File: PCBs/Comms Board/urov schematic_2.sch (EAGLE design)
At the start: 19 parts

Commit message: added ATTTINY84 and headers
started working on creating MAX4574 from scratch
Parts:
- added SL1: (no value), con-amp-quick:M02
- added SL2: (no value), con-amp-quick:M08
- added SL3: (no value), con-amp-quick:M04
- added U$3: ATTINY84ATTINY84-20PU, SparkFun-DigitalIC:ATTINY84ATTINY84-20PU
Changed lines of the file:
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@@
 <part name="J13" library="SparkFun-Connectors" deviceset="M04" device="PTH"/>
 <part name="J14" library="SparkFun-Connectors" deviceset="M02" device="PTH"/>
+<part name="U$3" library="SparkFun-DigitalIC" deviceset="ATTINY84" device="ATTINY84-20PU"/>
+<part name="SL1" library="con-amp-quick" deviceset="M02" device=""/>
+<part name="SL2" library="con-amp-quick" deviceset="M08" device=""/>
+<part name="SL3" library="con-amp-quick" deviceset="M04" device=""/>
 </parts>
 <sheets>
@@
 <instance part="J13" gate="G$1" x="-182.88" y="50.8"/>
 <instance part="J14" gate="G$1" x="-157.48" y="33.02"/>
+<instance part="U$3" gate="G$1" x="-5.08" y="137.16"/>
+<instance part="SL1" gate="G$1" x="-40.64" y="139.7"/>
+<instance part="SL2" gate="G$1" x="30.48" y="132.08" rot="R180"/>
+<instance part="SL3" gate="G$1" x="30.48" y="149.86" rot="R180"/>
 </instances>
 <busses>

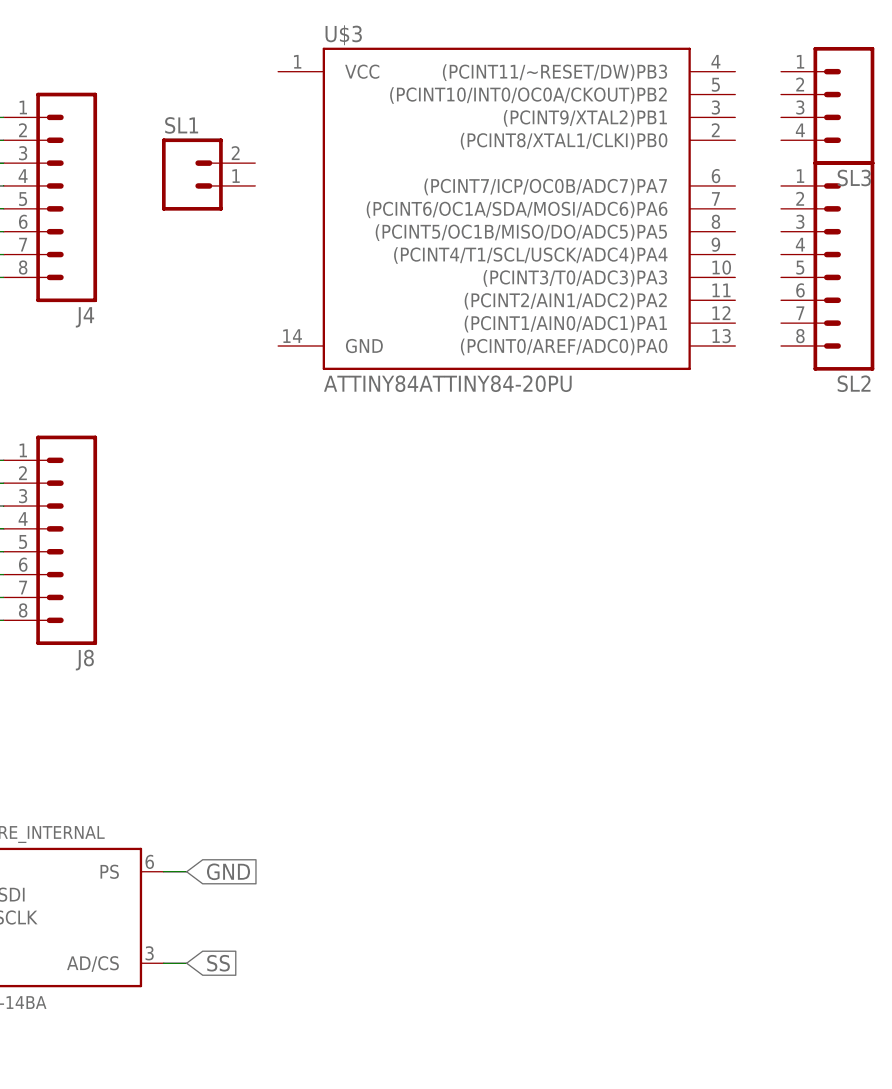
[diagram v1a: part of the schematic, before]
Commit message: added max4574
took forever
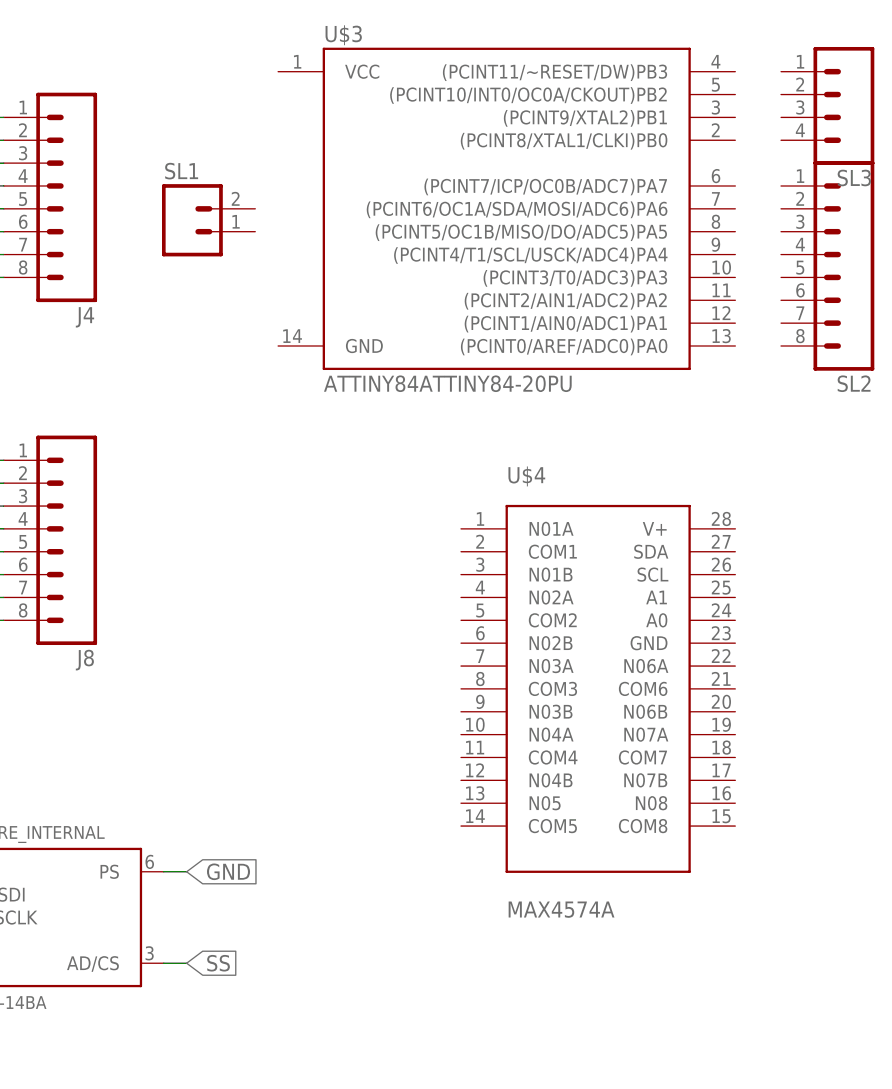
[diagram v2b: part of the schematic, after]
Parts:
- added U$4: MAX4574A, UROV_Accessories:MAX4574A
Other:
- moved on the sheet: SL1
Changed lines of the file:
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@@
 <part name="SL2" library="con-amp-quick" deviceset="M08" device=""/>
 <part name="SL3" library="con-amp-quick" deviceset="M04" device=""/>
+<part name="U$4" library="UROV_Accessories" deviceset="MAX4574" device="A"/>
 </parts>
 <sheets>
@@
 <instance part="J14" gate="G$1" x="-157.48" y="33.02"/>
 <instance part="U$3" gate="G$1" x="-5.08" y="137.16"/>
-<instance part="SL1" gate="G$1" x="-40.64" y="139.7"/>
+<instance part="SL1" gate="G$1" x="-40.64" y="134.62"/>
 <instance part="SL2" gate="G$1" x="30.48" y="132.08" rot="R180"/>
 <instance part="SL3" gate="G$1" x="30.48" y="149.86" rot="R180"/>
+<instance part="U$4" gate="G$1" x="5.08" y="83.82"/>
 </instances>
 <busses>

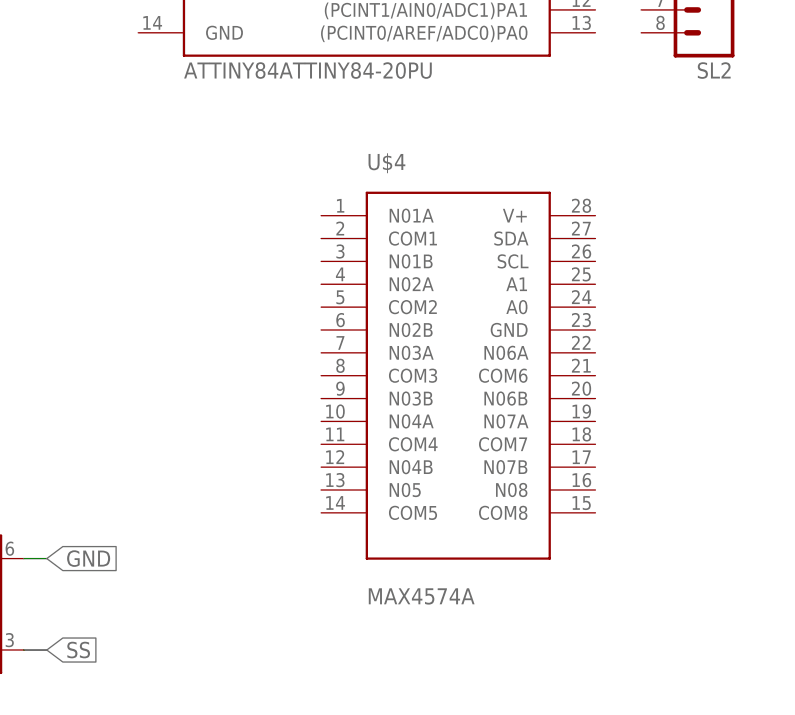
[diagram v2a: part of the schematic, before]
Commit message: updated board
rearranged board configuration, added wago screw clamps
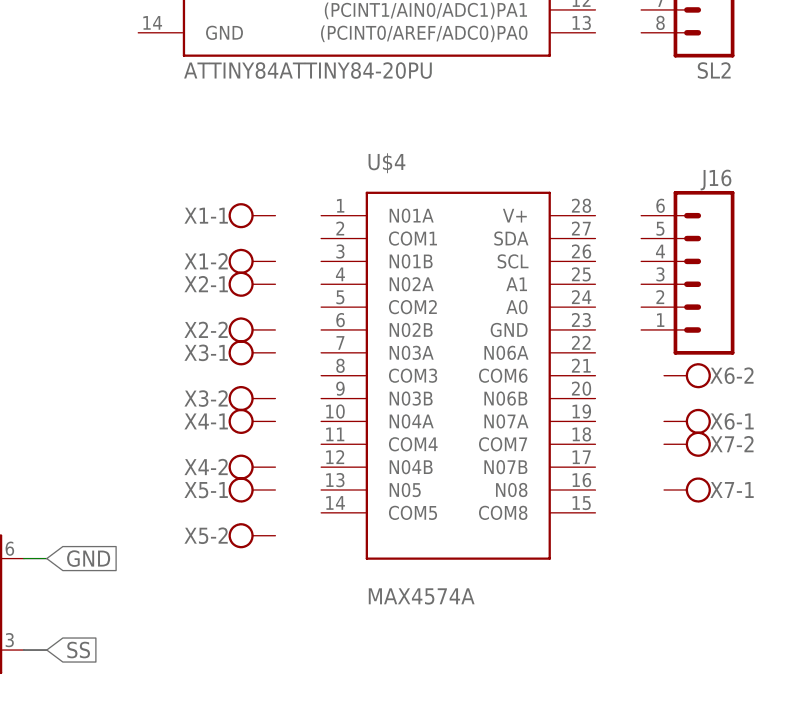
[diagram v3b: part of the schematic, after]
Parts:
- added J16: (no value), SparkFun-Connectors:M06POGOPIN_HOLES_ONLY
- added X1, X2, X3, X4, X5, X6, X7: (no value), con-wago-500:W237-102
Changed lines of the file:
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@@
 <part name="SL3" library="con-amp-quick" deviceset="M04" device=""/>
 <part name="U$4" library="UROV_Accessories" deviceset="MAX4574" device="A"/>
+<part name="J16" library="SparkFun-Connectors" deviceset="M06" device="POGOPIN_HOLES_ONLY"/>
+<part name="X1" library="con-wago-500" deviceset="W237-102" device=""/>
+<part name="X2" library="con-wago-500" deviceset="W237-102" device=""/>
+<part name="X3" library="con-wago-500" deviceset="W237-102" device=""/>
+<part name="X4" library="con-wago-500" deviceset="W237-102" device=""/>
+<part name="X5" library="con-wago-500" deviceset="W237-102" device=""/>
+<part name="X6" library="con-wago-500" deviceset="W237-102" device=""/>
+<part name="X7" library="con-wago-500" deviceset="W237-102" device=""/>
 </parts>
 <sheets>
@@
 <instance part="SL3" gate="G$1" x="30.48" y="149.86" rot="R180"/>
 <instance part="U$4" gate="G$1" x="5.08" y="83.82"/>
+<instance part="J16" gate="G$1" x="30.48" y="93.98" rot="MR0"/>
+<instance part="X1" gate="-1" x="-20.32" y="101.6"/>
+<instance part="X1" gate="-2" x="-20.32" y="96.52"/>
+<instance part="X2" gate="-1" x="-20.32" y="93.98"/>
+<instance part="X2" gate="-2" x="-20.32" y="88.9"/>
+<instance part="X3" gate="-1" x="-20.32" y="86.36"/>
+<instance part="X3" gate="-2" x="-20.32" y="81.28"/>
+<instance part="X4" gate="-1" x="-20.32" y="78.74"/>
+<instance part="X4" gate="-2" x="-20.32" y="73.66"/>
+<instance part="X5" gate="-1" x="-20.32" y="71.12"/>
+<instance part="X5" gate="-2" x="-20.32" y="66.04"/>
+<instance part="X6" gate="-1" x="33.02" y="78.74" rot="R180"/>
+<instance part="X6" gate="-2" x="33.02" y="83.82" rot="R180"/>
+<instance part="X7" gate="-1" x="33.02" y="71.12" rot="R180"/>
+<instance part="X7" gate="-2" x="33.02" y="76.2" rot="R180"/>
 </instances>
 <busses>
